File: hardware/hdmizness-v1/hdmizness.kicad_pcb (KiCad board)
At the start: 2 copper layers, 85.6 x 54 mm, 66 parts, among them J1 HDMI_A_PCB, J2 USB_A_PCB, SW1 SW_Push, U1 F1C100s, U2 TDA19988, U3 W25Q128JVPIQ, U4 EA3058, Y1 24M

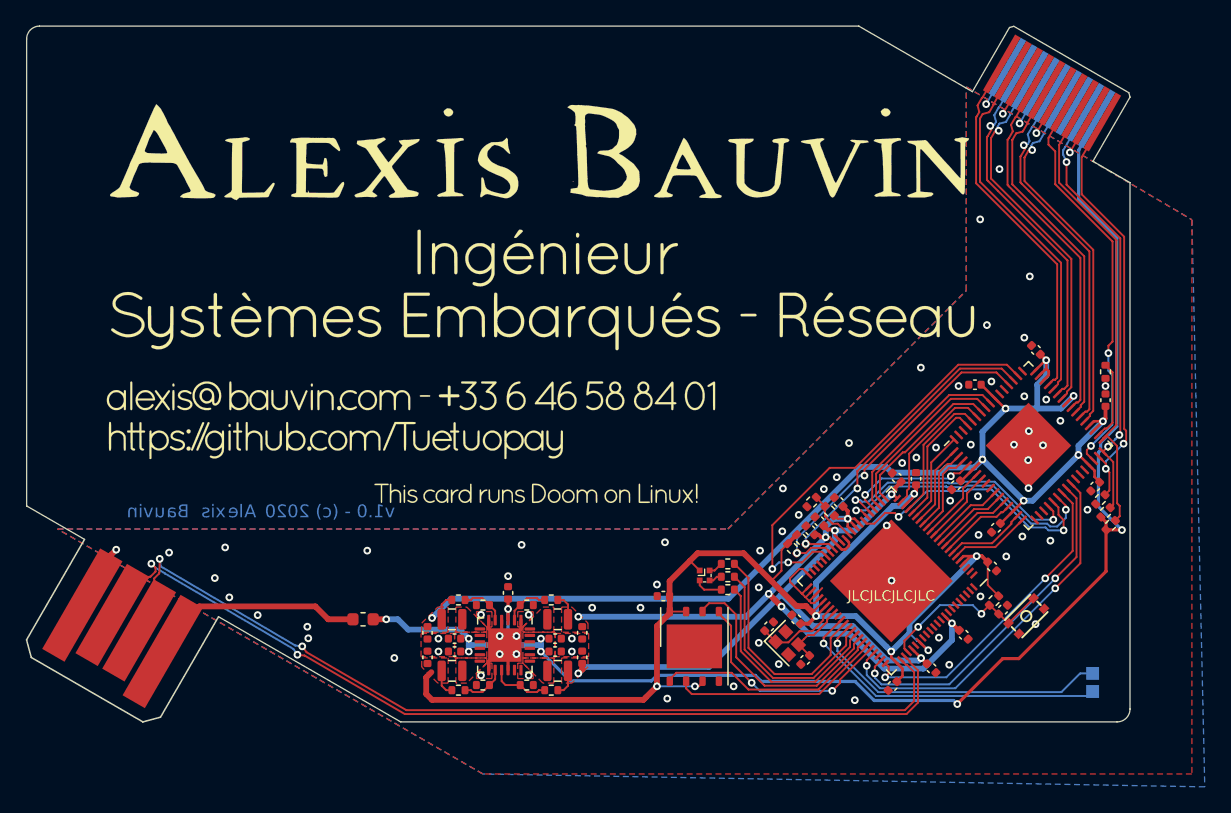
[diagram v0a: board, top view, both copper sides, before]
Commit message: hardware: update to KiCAD 9.0
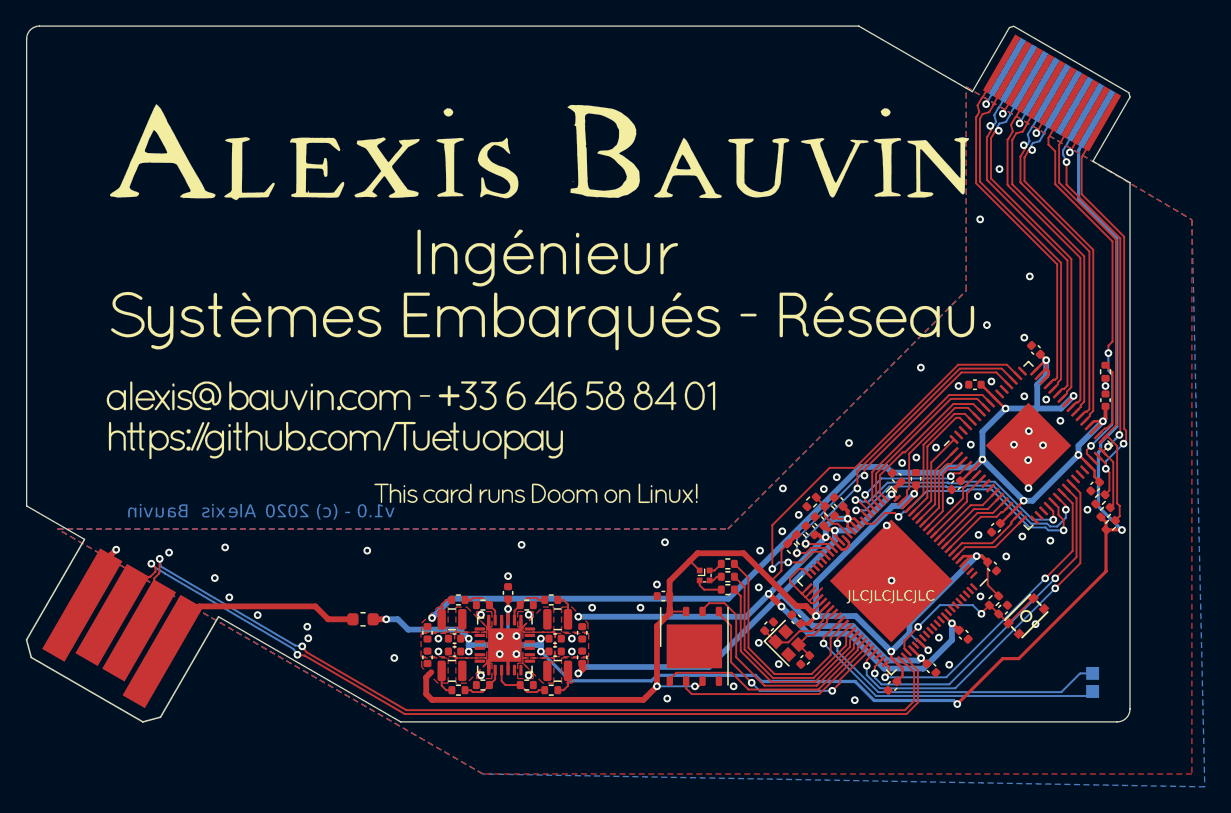
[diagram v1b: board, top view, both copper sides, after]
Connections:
- net /~RESET renamed /~{RESET}
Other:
- net class Default removed
- net class Power removed

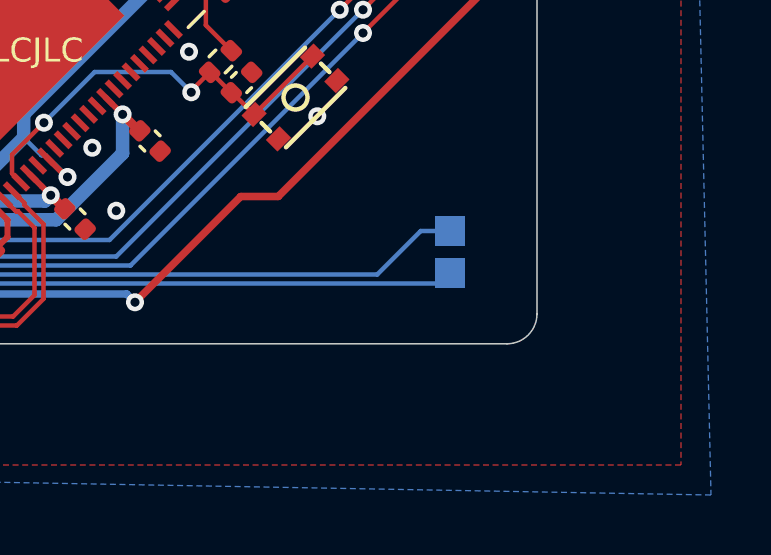
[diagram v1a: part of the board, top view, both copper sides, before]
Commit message: hardware: don't put soldermask in front of pcb connectors
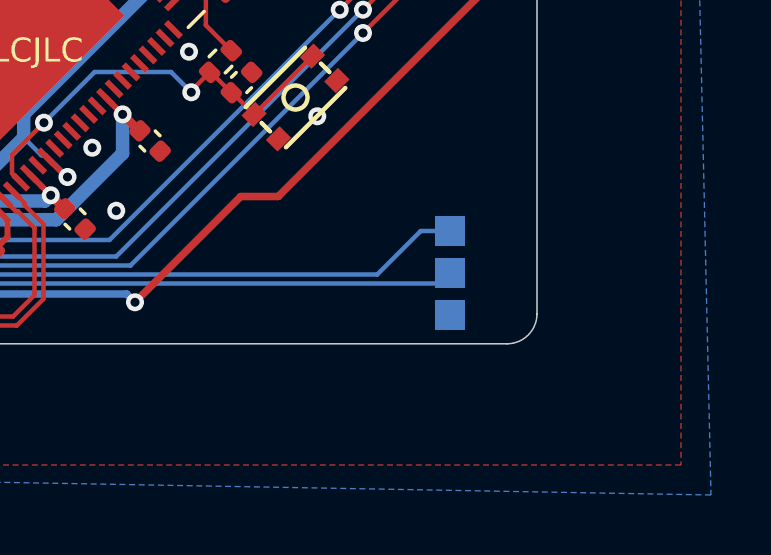
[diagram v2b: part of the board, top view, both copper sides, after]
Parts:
- added TP3: GND, TestPoint:TestPoint_Pad_1.0x1.0mm, B.Cu at (168.3, 107.0)
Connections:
- J1 pad 14: Net-(J1-Pad14) -> unconnected-(J1-UTILITY-Pad14)
- U1 pad 1: Net-(U1-Pad1) -> unconnected-(U1A-HPL-Pad1)
- U1 pad 2: Net-(U1-Pad2) -> unconnected-(U1A-HPCOMFB-Pad2)
- U1 pad 3: Net-(U1-Pad3) -> unconnected-(U1A-HPCOM-Pad3)
- U1 pad 40: Net-(U1-Pad40) -> unconnected-(U1A-PE9/CSI_D6/UART2_RTS/SPI1_CLK/EINTE9-Pad40)
- U1 pad 41: Net-(U1-Pad41) -> unconnected-(U1A-PE8/CSI_D5/UART2_RX/SPI1_MOSI/EINTE8-Pad41)
- U1 pad 42: Net-(U1-Pad42) -> unconnected-(U1A-PE7/CSI_D4/UART2_TX/SPI1_CS/EINTE7-Pad42)
- U1 pad 43: Net-(U1-Pad43) -> unconnected-(U1A-PE6/CSI_D3/PWM1/DA_OUT/OWA_OUT/EINTE6-Pad43)
- U1 pad 53: Net-(U1-Pad53) -> unconnected-(U1A-PF5/SDC0_D2/DBG_CK/PWM1/EINTF5-Pad53)
- U1 pad 64: Net-(U1-Pad64) -> unconnected-(U1A-PA2/TPY1/PWM0/DA_IN/UART1_RX/SPI1_CLK-Pad64)
- U1 pad 72: Net-(U1-Pad72) -> unconnected-(U1A-TVOUT-Pad72)
- U1 pad 75: Net-(U1-Pad75) -> unconnected-(U1A-TV_VRN-Pad75)
- U1 pad 76: Net-(U1-Pad76) -> unconnected-(U1A-TV_VRP-Pad76)
- U1 pad 77: Net-(U1-Pad77) -> unconnected-(U1A-TVIN1-Pad77)
- U1 pad 78: Net-(U1-Pad78) -> unconnected-(U1A-TVIN0-Pad78)
- U1 pad 79: Net-(U1-Pad79) -> unconnected-(U1A-LRADC0-Pad79)
- U1 pad 81: Net-(U1-Pad81) -> unconnected-(U1A-VRA1-Pad81)
- U1 pad 83: Net-(U1-Pad83) -> unconnected-(U1A-VRA2-Pad83)
- U1 pad 84: Net-(U1-Pad84) -> unconnected-(U1A-FMINL-Pad84)
- U1 pad 85: Net-(U1-Pad85) -> unconnected-(U1A-FMINR-Pad85)
- U1 pad 86: Net-(U1-Pad86) -> unconnected-(U1A-LINEIN-Pad86)
- U1 pad 87: Net-(U1-Pad87) -> unconnected-(U1A-MICIN-Pad87)
- U1 pad 88: Net-(U1-Pad88) -> unconnected-(U1A-HPR-Pad88)
- U2 pad 26: Net-(U2-Pad26) -> unconnected-(U2-AP2-Pad26)
- U2 pad 27: Net-(U2-Pad27) -> unconnected-(U2-AP3/OSC_IN-Pad27)
- U2 pad 28: Net-(U2-Pad28) -> unconnected-(U2-AP4-Pad28)
- U4 pad 17: Net-(U4-Pad17) -> unconnected-(U4-NC-Pad17)
- U4 pad 18: Net-(U4-Pad18) -> unconnected-(U4-NC-Pad18)
